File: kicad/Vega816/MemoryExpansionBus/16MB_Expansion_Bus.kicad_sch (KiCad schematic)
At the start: 9 parts, among them J35 RAM_CS, J36 Conn_02x40_Odd_Even, J37 CPU, J38 Conn_02x40_Odd_Even, J39 Conn_02x40_Odd_Even, J40 Conn_02x40_Odd_Even, J41 Conn_02x40_Odd_Even, U32 74ACH138, U33 74HC32

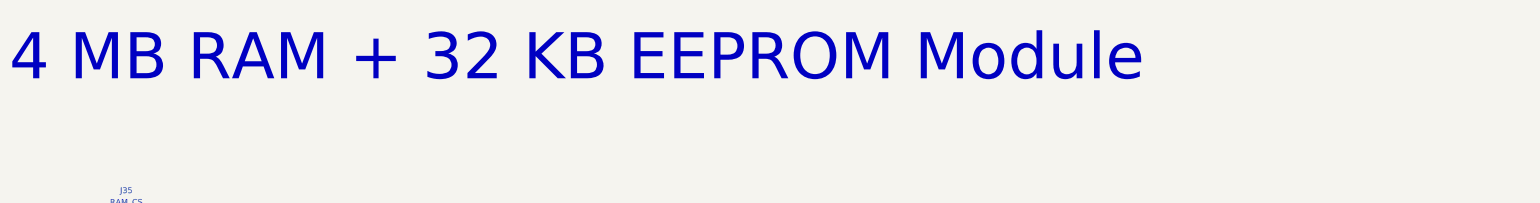
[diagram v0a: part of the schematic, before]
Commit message: expansion bus breakout
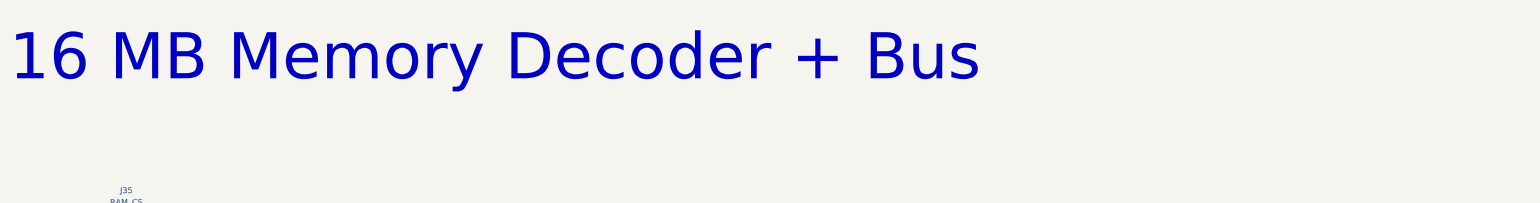
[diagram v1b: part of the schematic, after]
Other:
- note added: "16 MB Memory Decoder + Bus"
- note removed: "4 MB RAM + 32 KB EEPROM Module"
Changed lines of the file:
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@@
     (effects (font (size 3 3)) (justify left bottom))
   )
-  (text "4 MB RAM + 32 KB EEPROM Module" (at 29.21 43.18 0)
+  (text "16 MB Memory Decoder + Bus" (at 29.21 43.18 0)
     (effects (font (size 10 10)) (justify left bottom))
   )

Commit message: new plots
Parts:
- removed unit 1 of U33
- added R?: 10K, symbol Device:R
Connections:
- net VCC: now also R?.1; no longer U32.6 (E3)
- net ~{CS}: now also U32.15 (O0)
- net IO_AREA renamed ~{IO_AREA}
- net ~{IO_AREA}: now also U32.6 (E3), R?.2
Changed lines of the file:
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@@
   (junction (at 246.38 154.94) (diameter 0) (color 0 0 0 0)
   )
+  (junction (at 86.36 72.39) (diameter 0) (color 0 0 0 0)
+  )
   (junction (at 124.46 172.72) (diameter 0) (color 0 0 0 0)
   )
@@
     (stroke (width 0) (type default) (color 0 0 0 0))
   )
-  (wire (pts (xy 60.96 72.39) (xy 124.46 72.39))
+  (wire (pts (xy 60.96 72.39) (xy 86.36 72.39))
     (stroke (width 0) (type default) (color 0 0 0 0))
   )
@@
     (stroke (width 0) (type default) (color 0 0 0 0))
   )
-  (wire (pts (xy 86.36 106.68) (xy 86.36 104.14))
+  (wire (pts (xy 86.36 72.39) (xy 86.36 106.68))
     (stroke (width 0) (type default) (color 0 0 0 0))
   )
@@
     (stroke (width 0) (type default) (color 0 0 0 0))
   )
-  (wire (pts (xy 124.46 72.39) (xy 124.46 91.44))
-    (stroke (width 0) (type default) (color 0 0 0 0))
-  )
   (wire (pts (xy 144.78 180.34) (xy 139.7 180.34))
     (stroke (width 0) (type default) (color 0 0 0 0))
@@
     (stroke (width 0) (type default) (color 0 0 0 0))
   )
-  (wire (pts (xy 142.24 93.98) (xy 266.7 93.98))
+  (wire (pts (xy 120.65 96.52) (xy 266.7 96.52))
     (stroke (width 0) (type default) (color 0 0 0 0))
   )
@@
     (stroke (width 0) (type default) (color 0 0 0 0))
   )
-  (wire (pts (xy 266.7 93.98) (xy 266.7 137.16))
+  (wire (pts (xy 266.7 96.52) (xy 266.7 137.16))
     (stroke (width 0) (type default) (color 0 0 0 0))
   )
@@
     (stroke (width 0) (type default) (color 0 0 0 0))
   )
-  (wire (pts (xy 120.65 96.52) (xy 127 96.52))
-    (stroke (width 0) (type default) (color 0 0 0 0))
-  )
   (wire (pts (xy 226.06 228.6) (xy 220.98 228.6))
     (stroke (width 0) (type default) (color 0 0 0 0))
@@
     (stroke (width 0) (type default) (color 0 0 0 0))
   )
-  (wire (pts (xy 124.46 91.44) (xy 127 91.44))
-    (stroke (width 0) (type default) (color 0 0 0 0))
-  )
   (wire (pts (xy 124.46 149.86) (xy 127 149.86))
     (stroke (width 0) (type default) (color 0 0 0 0))
@@
     (effects (font (size 1.27 1.27)) (justify left bottom))
   )
-  (label "IO_AREA" (at 60.96 72.39 0)
+  (label "~{IO_AREA}" (at 60.96 72.39 0)
     (effects (font (size 1.27 1.27)) (justify left bottom))
   )
@@
     (pin "1")
   )
+  (symbol (lib_name "VCC_1") (lib_id "power:VCC") (at 86.36 64.77 0) (mirror y) (unit 1)
+    (in_bom yes) (on_board yes)
+    (property "Reference" "#PWR?" (id 0) (at 86.36 68.58 0)
+      (effects (font (size 1.27 1.27)) hide)
+    )
+    (property "Value" "VCC" (id 1) (at 86.36 60.325 0))
+    (property "Footprint" "" (id 2) (at 86.36 64.77 0)
+      (effects (font (size 1.27 1.27)) hide)
+    )
+    (property "Datasheet" "" (id 3) (at 86.36 64.77 0)
+      (effects (font (size 1.27 1.27)) hide)
+    )
+    (pin "1")
+  )
   (symbol (lib_id "Connector_Generic:Conn_02x40_Odd_Even") (at 55.88 134.62 0) (mirror y) (unit 1)
     (in_bom yes) (on_board yes)
@@
     (pin "9")
   )
+  (symbol (lib_id "Device:R") (at 86.36 68.58 0) (unit 1)
+    (in_bom yes) (on_board yes) (fields_autoplaced)
+    (property "Reference" "R?" (id 0) (at 88.9 67.3099 0)
+      (effects (font (size 1.27 1.27)) (justify left))
+    )
+    (property "Value" "10K" (id 1) (at 88.9 69.8499 0)
+      (effects (font (size 1.27 1.27)) (justify left))
+    )
+    (property "Footprint" "" (id 2) (at 84.582 68.58 90)
+      (effects (font (size 1.27 1.27)) hide)
+    )
+    (property "Datasheet" "~" (id 3) (at 86.36 68.58 0)
+      (effects (font (size 1.27 1.27)) hide)
+    )
+    (pin "1")
+    (pin "2")
+  )
   (symbol (lib_id "power:GND") (at 45.72 231.14 0) (unit 1)
     (in_bom yes) (on_board yes)
@@
     (pin "7")
   )
-  (symbol (lib_id "Vega816:74HC32") (at 134.62 93.98 0) (unit 1)
-    (in_bom yes) (on_board yes) (fields_autoplaced)
-    (property "Reference" "U33" (id 0) (at 134.62 85.09 0))
-    (property "Value" "74HC32" (id 1) (at 134.62 87.63 0))
-    (property "Footprint" "" (id 2) (at 134.62 93.98 0)
-      (effects (font (size 1.27 1.27)) hide)
-    )
-    (property "Datasheet" "https://www.diodes.com/assets/Datasheets/74HC32.pdf" (id 3) (at 134.62 93.98 0)
-      (effects (font (size 1.27 1.27)) hide)
-    )
-    (pin "1")
-    (pin "2")
-    (pin "3")
-    (pin "4")
-    (pin "5")
-    (pin "6")
-    (pin "10")
-    (pin "8")
-    (pin "9")
-    (pin "11")
-    (pin "12")
-    (pin "13")
-    (pin "14")
-    (pin "7")
-  )
   (symbol (lib_name "GND_2") (lib_id "power:GND") (at 246.38 231.14 0) (unit 1)
     (in_bom yes) (on_board yes)
@@
       (effects (font (size 1.27 1.27)) hide)
     )
-    (pin "1")
-  )
-  (symbol (lib_name "VCC_1") (lib_id "power:VCC") (at 86.36 104.14 0) (mirror y) (unit 1)
-    (in_bom yes) (on_board yes)
-    (property "Reference" "#PWR044" (id 0) (at 86.36 107.95 0)
-      (effects (font (size 1.27 1.27)) hide)
-    )
-    (property "Value" "VCC" (id 1) (at 86.36 99.695 0))
-    (property "Footprint" "" (id 2) (at 86.36 104.14 0)
-      (effects (font (size 1.27 1.27)) hide)
-    )
-    (property "Datasheet" "" (id 3) (at 86.36 104.14 0)
-      (effects (font (size 1.27 1.27)) hide)
-    )

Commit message: Big push, Sysctl, DMA Reg
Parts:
- renumbered J37 to J?, J39 to J?, J36 to J?, J41 to J?, J38 to J?, J35 to J?, J40 to J?, U33 to U?, U32 to U?
